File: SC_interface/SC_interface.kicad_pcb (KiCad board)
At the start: 2 copper layers, 118 parts, among them J101 5V_PWR, J102 J_chassis, J201 Input, J202 BalancedOut, J203 Output_BNC, J301 Input, J302 BalancedOut, J303 Output_BNC, Q201 LND150N8, Q202 LND150N8, Q203 LND150N8, Q204 LND150N8, Q301 LND150N8, Q302 LND150N8, Q303 LND150N8, Q304 LND150N8, SW101 Main Power, SW102 Master SW, SW201 SW_Select1, SW301 SW_Select1, U101 JCA0305D03, U201 DRV135UA, U202 U2 OPA1656IDR, U203 INA134UA, U301 DRV135UA, U302 U2 OPA1656IDR, U303 INA134UA

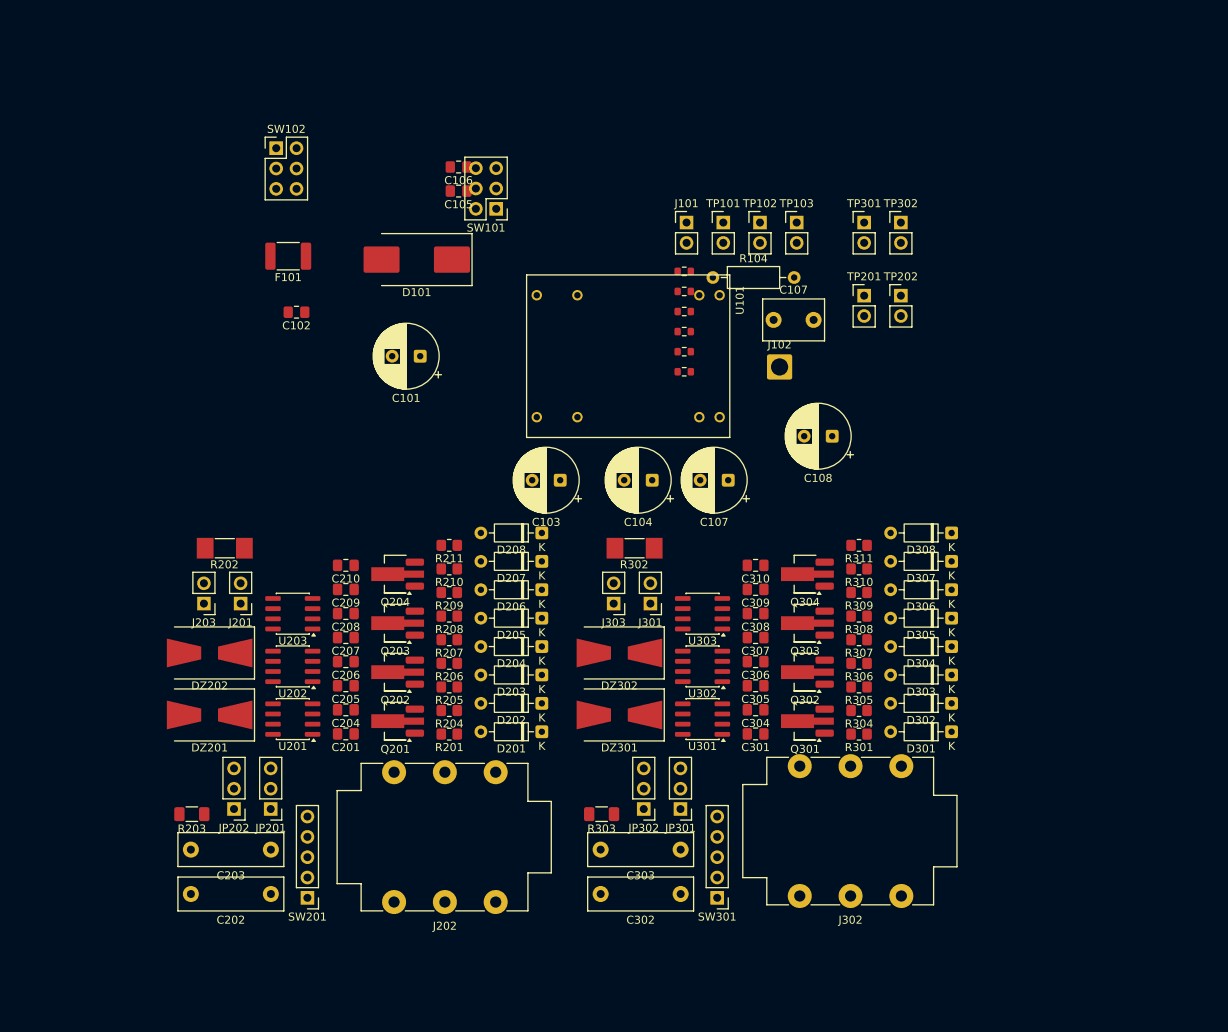
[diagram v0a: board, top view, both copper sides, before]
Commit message: schematic changes
1. added TVS at output of DC-DC convert to prevent kick back
2. Changed all diodes to BAV199
3. change the Cfeedback to 4.7uF
4. removed LND Fet, replaced it with 4.7 K ohm
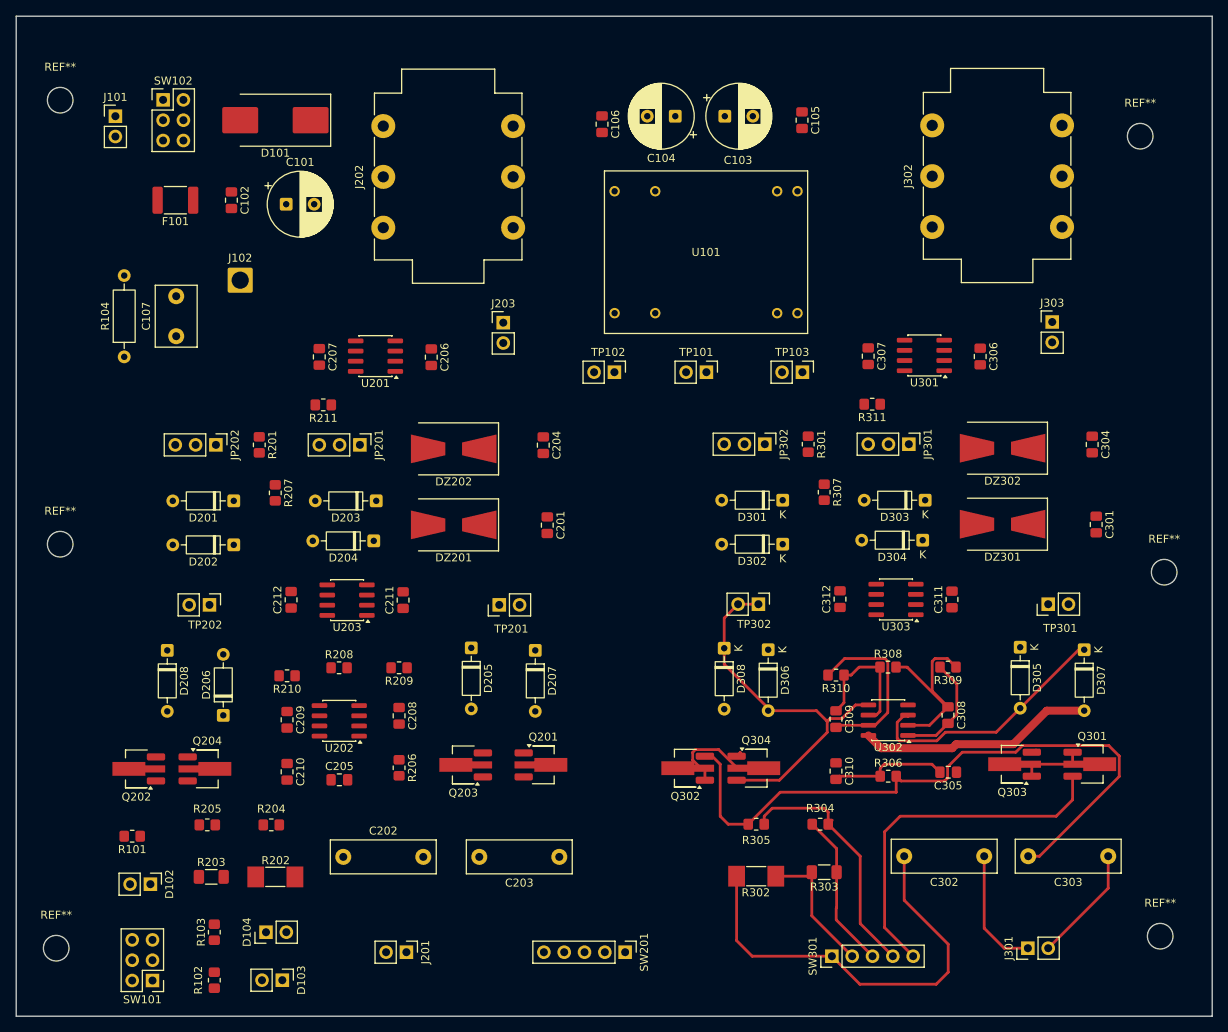
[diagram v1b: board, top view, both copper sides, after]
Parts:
- removed the C107 at (109.5, 83.0)
- removed C108: 330uf 25V, Capacitor_THT:CP_Radial_D8.0mm_P3.50mm
- added C211: 0.1uf, Capacitor_SMD:C_0805_2012Metric_Pad1.18x1.45mm_HandSolder, F.Cu at (68.9, 98.0)
- added C212: 0.1uf, Capacitor_SMD:C_0805_2012Metric_Pad1.18x1.45mm_HandSolder, F.Cu at (54.9, 98.0)
- added C311: 0.1uf, Capacitor_SMD:C_0805_2012Metric_Pad1.18x1.45mm_HandSolder, F.Cu at (137.5, 97.9)
- added C312: 0.1uf, Capacitor_SMD:C_0805_2012Metric_Pad1.18x1.45mm_HandSolder, F.Cu at (123.5, 97.9)
- added REF**: MountingHole_3.2mm_M3, MountingHole:MountingHole_3.2mm_M3, F.Cu at (25.5, 141.5)
- added REF**: MountingHole_3.2mm_M3, MountingHole:MountingHole_3.2mm_M3, F.Cu at (161.0, 40.0)
- added REF**: MountingHole_3.2mm_M3, MountingHole:MountingHole_3.2mm_M3, F.Cu at (26.0, 91.0)
- added REF**: MountingHole_3.2mm_M3, MountingHole:MountingHole_3.2mm_M3, F.Cu at (26.0, 35.5)
- added REF**: MountingHole_3.2mm_M3, MountingHole:MountingHole_3.2mm_M3, F.Cu at (164.0, 94.5)
- added REF**: MountingHole_3.2mm_M3, MountingHole:MountingHole_3.2mm_M3, F.Cu at (163.5, 140.0)
- D102, D103, D104: footprint PCM_SparkFun-Resistor:R_0603_1608Metric -> Connector_PinHeader_2.54mm:PinHeader_1x02_P2.54mm_Vertical
- R101, R102, R103: footprint PCM_SparkFun-Resistor:R_0603_1608Metric -> Resistor_SMD:R_0805_2012Metric_Pad1.20x1.40mm_HandSolder
- moved SW101 105.6 mm to (37.5, 145.5)
- moved D102 101.6 mm to (37.3, 133.5), turned to -90 degrees
- moved D103 99.7 mm to (53.8, 145.5), turned to -90 degrees
- moved R102 98.1 mm to (45.3, 145.5), turned to -90 degrees
- moved TP202 94.7 mm to (44.7, 98.6), turned to -90 degrees
- moved D104 93.6 mm to (51.7, 139.5), turned to 90 degrees
- moved R101 93.5 mm to (35.0, 127.5), turned to 180 degrees
- moved R103 91.4 mm to (45.3, 139.5), turned to 90 degrees
- moved J202 85.5 mm to (66.4, 51.4), turned to 90 degrees
- moved J302 83.7 mm to (135.0, 51.4), turned to 90 degrees
- moved C107 74.7 mm to (40.5, 65.0), turned to 90 degrees
- moved R104 74.2 mm to (34.0, 67.6), turned to 90 degrees
- moved J101 72.6 mm to (32.9, 37.5)
- moved J102 68.3 mm to (48.5, 58.0)
- moved J303 65.1 mm to (150.0, 63.2), turned to 0 degrees
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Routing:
- net Net-(Q302-D): track 0.00 -> 84.3 mm
- net Net-(C302-Pad2): track 0.00 -> 54.2 mm
- net Net-(D306-A): track 0.00 -> 48.0 mm
- net Net-(Q301-D): track 0.00 -> 45.1 mm
- net Net-(D305-A): track 0.00 -> 32.9 mm
- net Net-(R304-Pad1): track 0.00 -> 31.7 mm
- net +VDC: track 0.00 -> 29.6 mm
- net Net-(U302A--): track 0.00 -> 24.6 mm
- net Net-(U303-IN-): track 0.00 -> 22.1 mm
- net Net-(R303-Pad1): track 0.00 -> 19.7 mm
- net Net-(R302-Pad1): track 0.00 -> 17.3 mm
- net Net-(U302B--): track 0.00 -> 17.0 mm
- net Net-(J301-In): track 0.00 -> 15.5 mm
- net GND: track 0.00 -> 14.8 mm
- net Net-(J301-Ext): track 0.00 -> 14.6 mm
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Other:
- board outline added: 149.5 x 125 mm
